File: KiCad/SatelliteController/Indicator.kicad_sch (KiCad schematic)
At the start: 22 parts

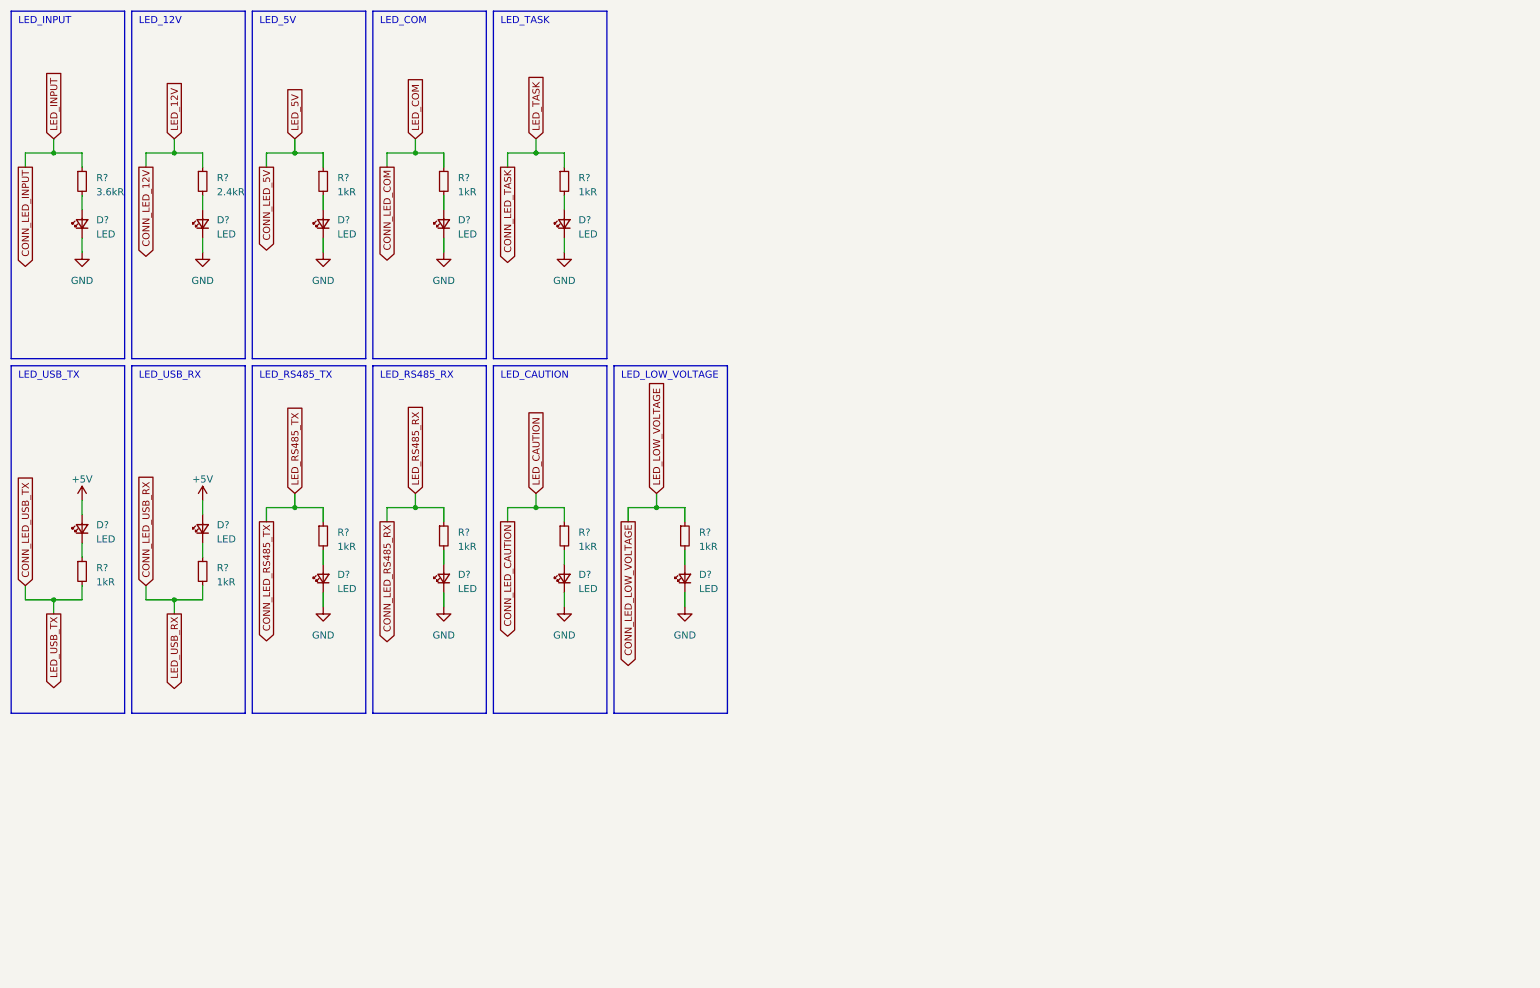
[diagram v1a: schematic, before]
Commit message: ランコンのKiCadプロジェクトをコピーしてサテコンを作成
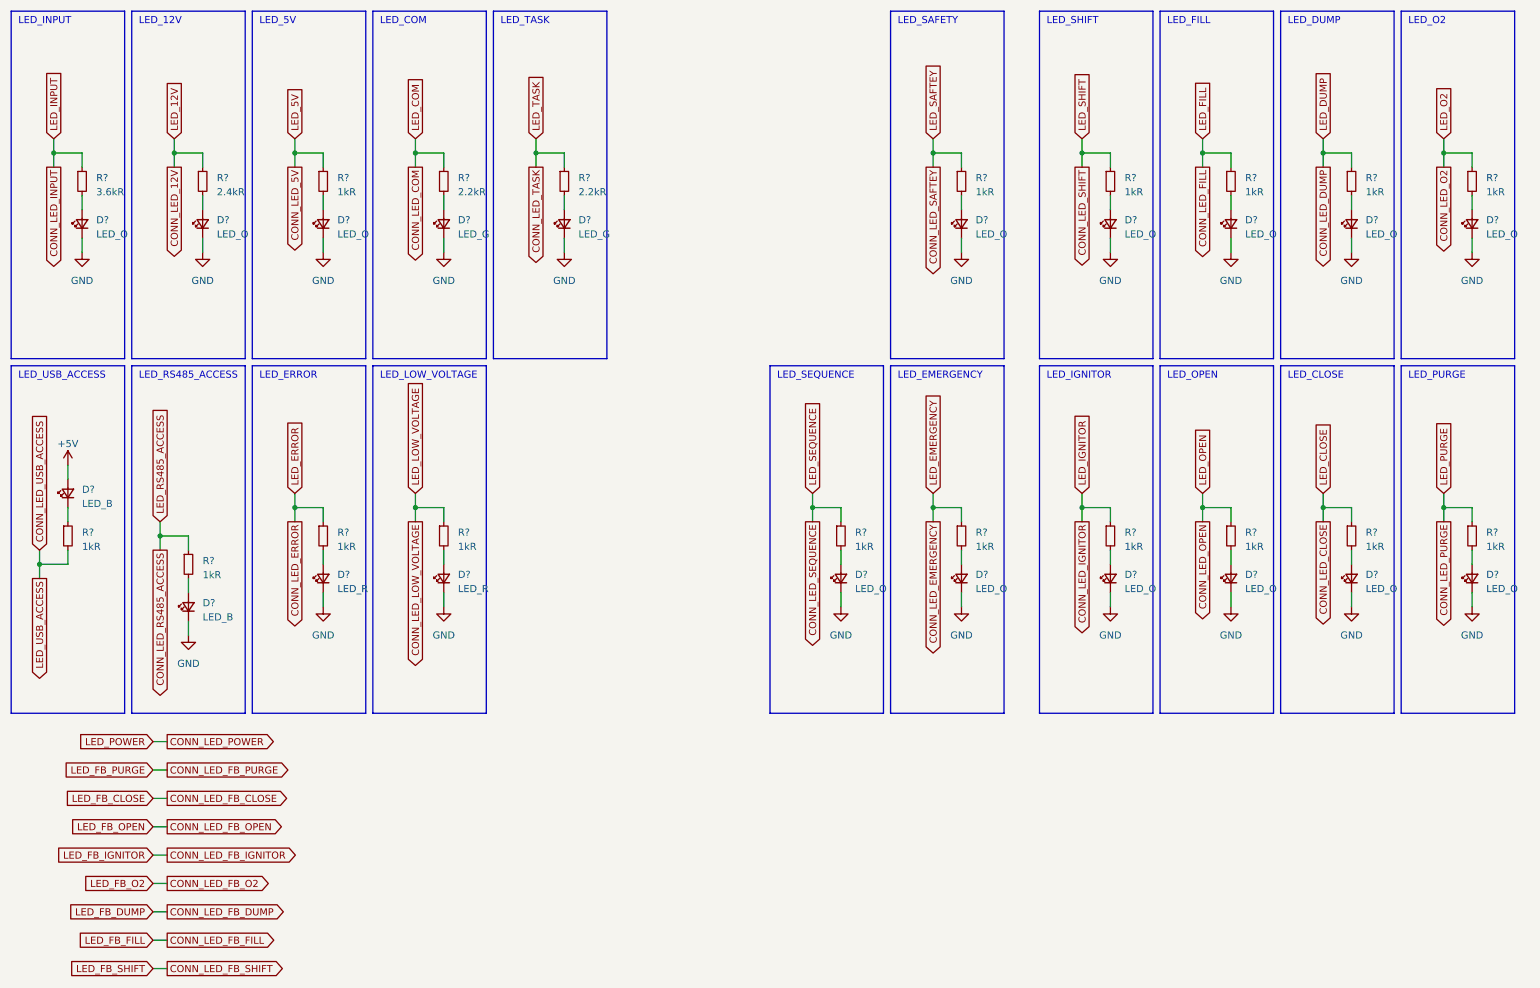
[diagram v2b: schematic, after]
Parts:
- removed D? (x2): LED, LED_SMD:LED_0603_1608Metric_Pad1.05x0.95mm_HandSolder, symbol Device:LED_Small
- removed R? (x2): 1kR, Resistor_SMD:R_0603_1608Metric_Pad0.98x0.95mm_HandSolder, symbol Device:R_Small
- added D? (x11): LED_O, LED_SMD:LED_0603_1608Metric_Pad1.05x0.95mm_HandSolder, symbol Device:LED_Small
- added R? (x11): 1kR, Resistor_SMD:R_0603_1608Metric_Pad0.98x0.95mm_HandSolder, symbol Device:R_Small
- D? (x2): value LED -> LED_R
- D? (x3): value LED -> LED_O
- D? (x2): value LED -> LED_B
- D? (x2): value LED -> LED_G
- R? (x2): value 1kR -> 2.2kR
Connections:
- net GND: now also D?.1 (K), D?.1 (K), D?.1 (K), D?.1 (K), D?.1 (K), D?.1 (K), D?.1 (K), D?.1 (K), D?.1 (K), D?.1 (K), D?.1 (K)
- net CONN_LED_CAUTION renamed CONN_LED_ERROR
- net CONN_LED_RS485_TX renamed CONN_LED_RS485_ACCESS
- net CONN_LED_USB_TX renamed CONN_LED_USB_ACCESS
- new net: D?.2 (A), R?.2 (x11)
- new net CONN_LED_CLOSE: R?.1
- new net CONN_LED_DUMP: R?.1
- new net CONN_LED_EMERGENCY: R?.1
- new net CONN_LED_FILL: R?.1
- new net CONN_LED_IGNITOR: R?.1
- new net CONN_LED_O2: R?.1
- new net CONN_LED_OPEN: R?.1
- new net CONN_LED_PURGE: R?.1
- new net CONN_LED_SAFTEY: R?.1
- new net CONN_LED_SEQUENCE: R?.1
- new net CONN_LED_SHIFT: R?.1
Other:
- note added: "LED_CLOSE"
- note added: "LED_DUMP"
- note added: "LED_EMERGENCY"
- note added: "LED_ERROR"
- note added: "LED_FILL"
- note added: "LED_IGNITOR"
- note added: "LED_O2"
- note added: "LED_OPEN"
- note added: "LED_PURGE"
- note added: "LED_RS485_ACCESS"
- note added: "LED_SAFETY"
- note added: "LED_SEQUENCE"
- note added: "LED_SHIFT"
- note added: "LED_USB_ACCESS"
- note removed: "LED_CAUTION"
- note removed: "LED_RS485_RX"
- note removed: "LED_RS485_TX"
- note removed: "LED_USB_RX"
- note removed: "LED_USB_TX"
- moved on the sheet: D?, R?

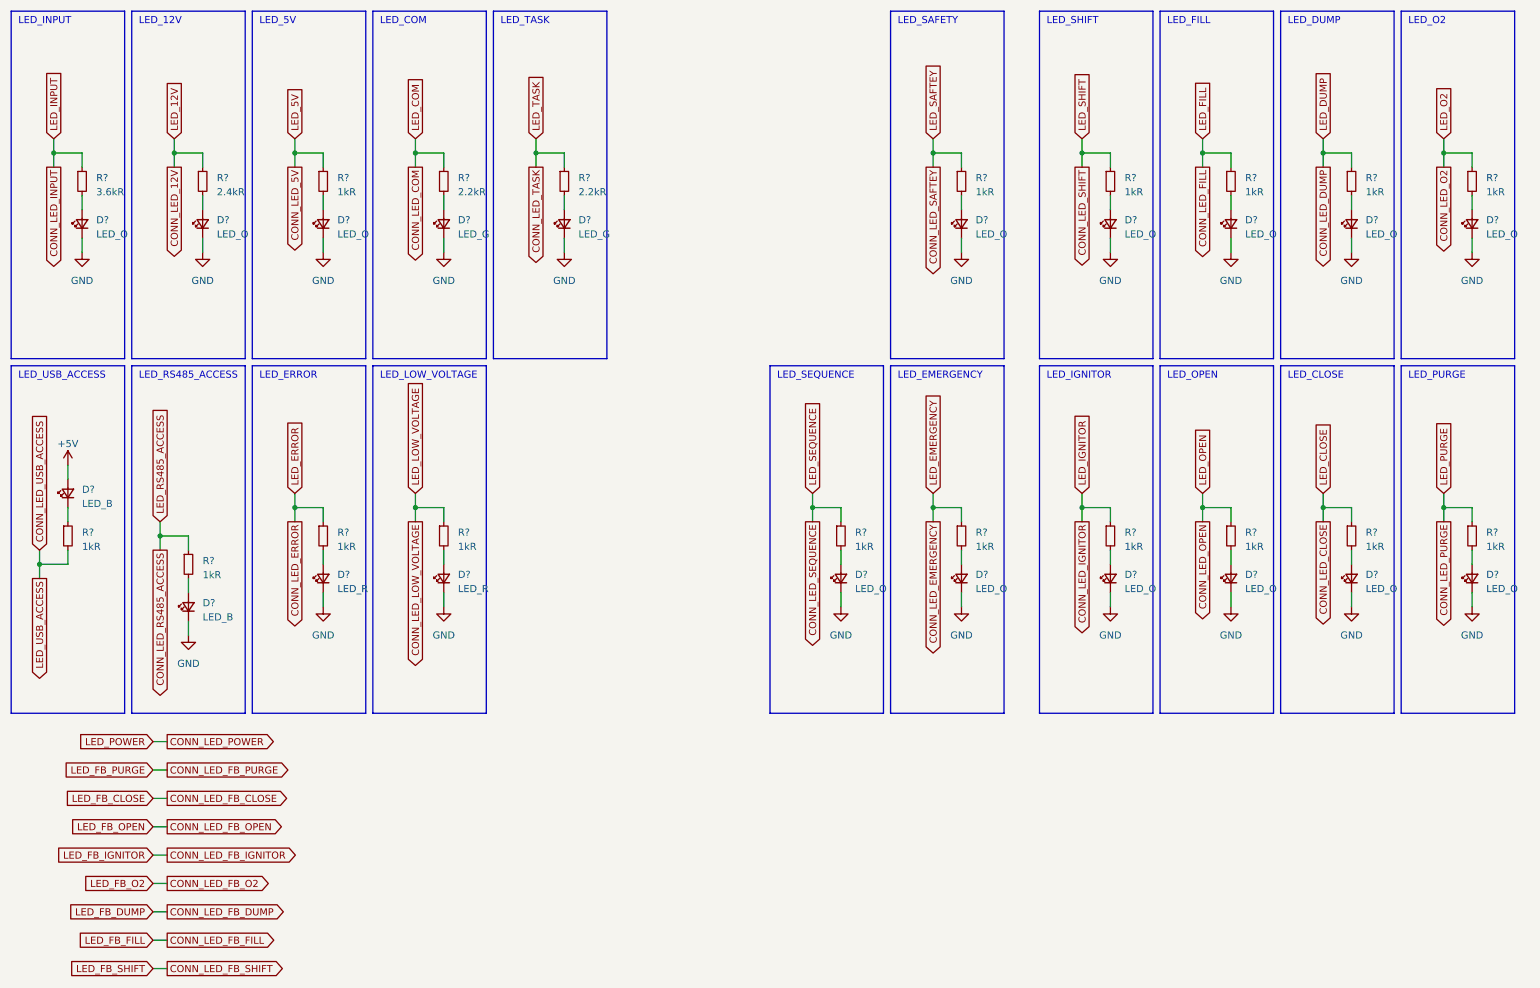
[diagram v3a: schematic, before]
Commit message: 手動操作を削除
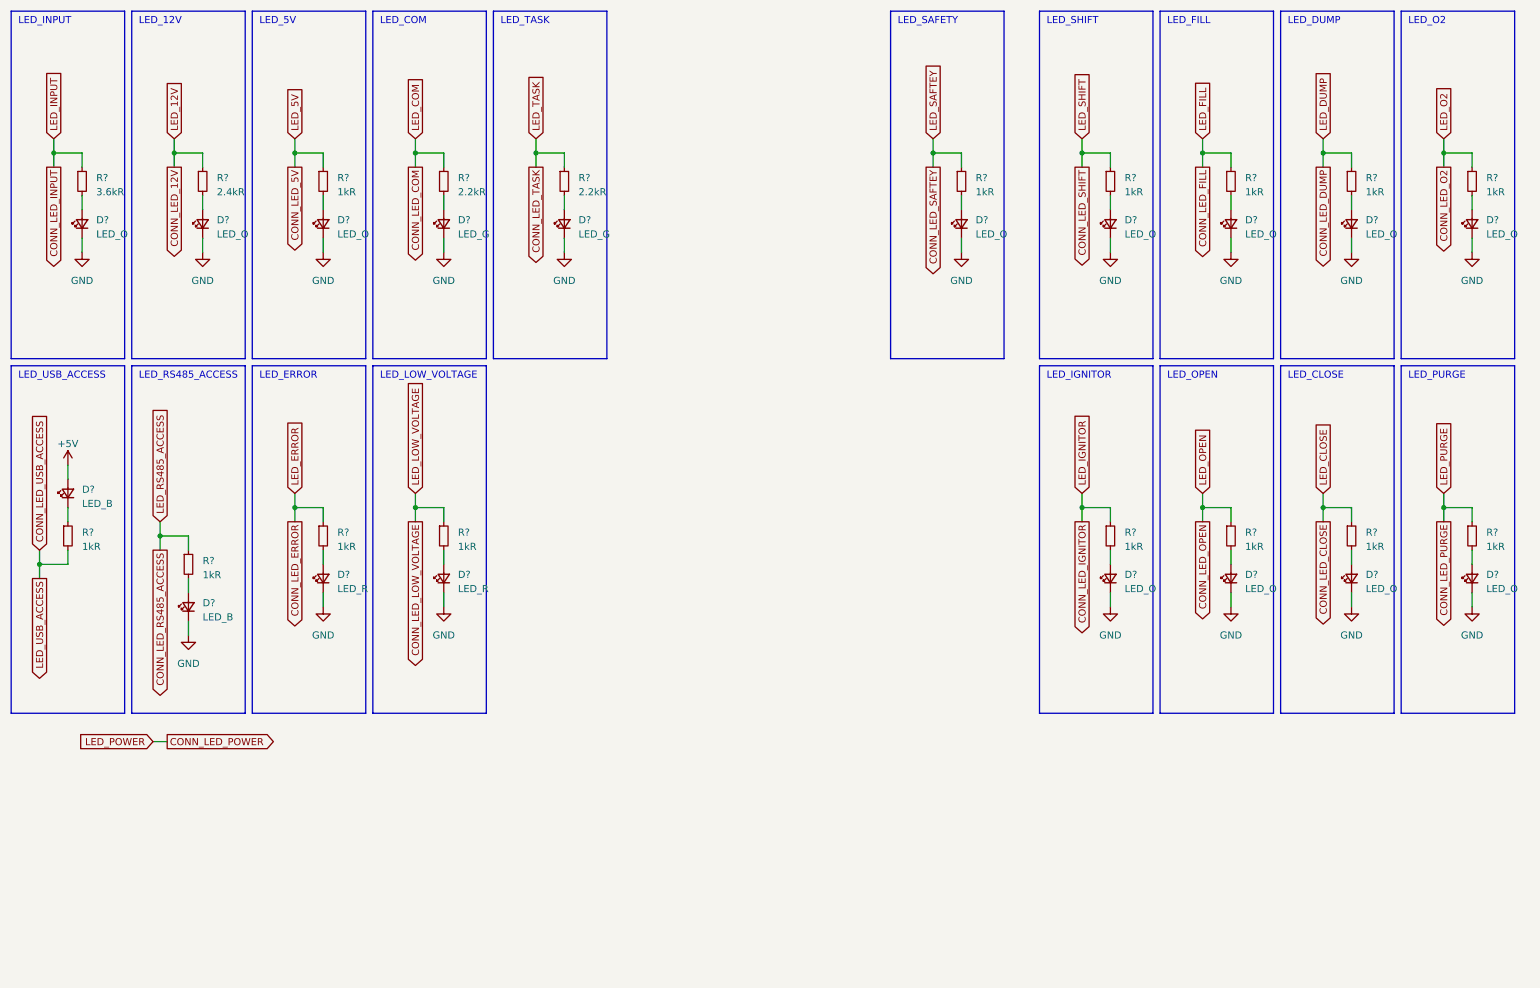
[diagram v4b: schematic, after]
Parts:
- removed D? (x2): LED_O, LED_SMD:LED_0603_1608Metric_Pad1.05x0.95mm_HandSolder, symbol Device:LED_Small
- removed R? (x2): 1kR, Resistor_SMD:R_0603_1608Metric_Pad0.98x0.95mm_HandSolder, symbol Device:R_Small
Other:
- note removed: "LED_EMERGENCY"
- note removed: "LED_SEQUENCE"

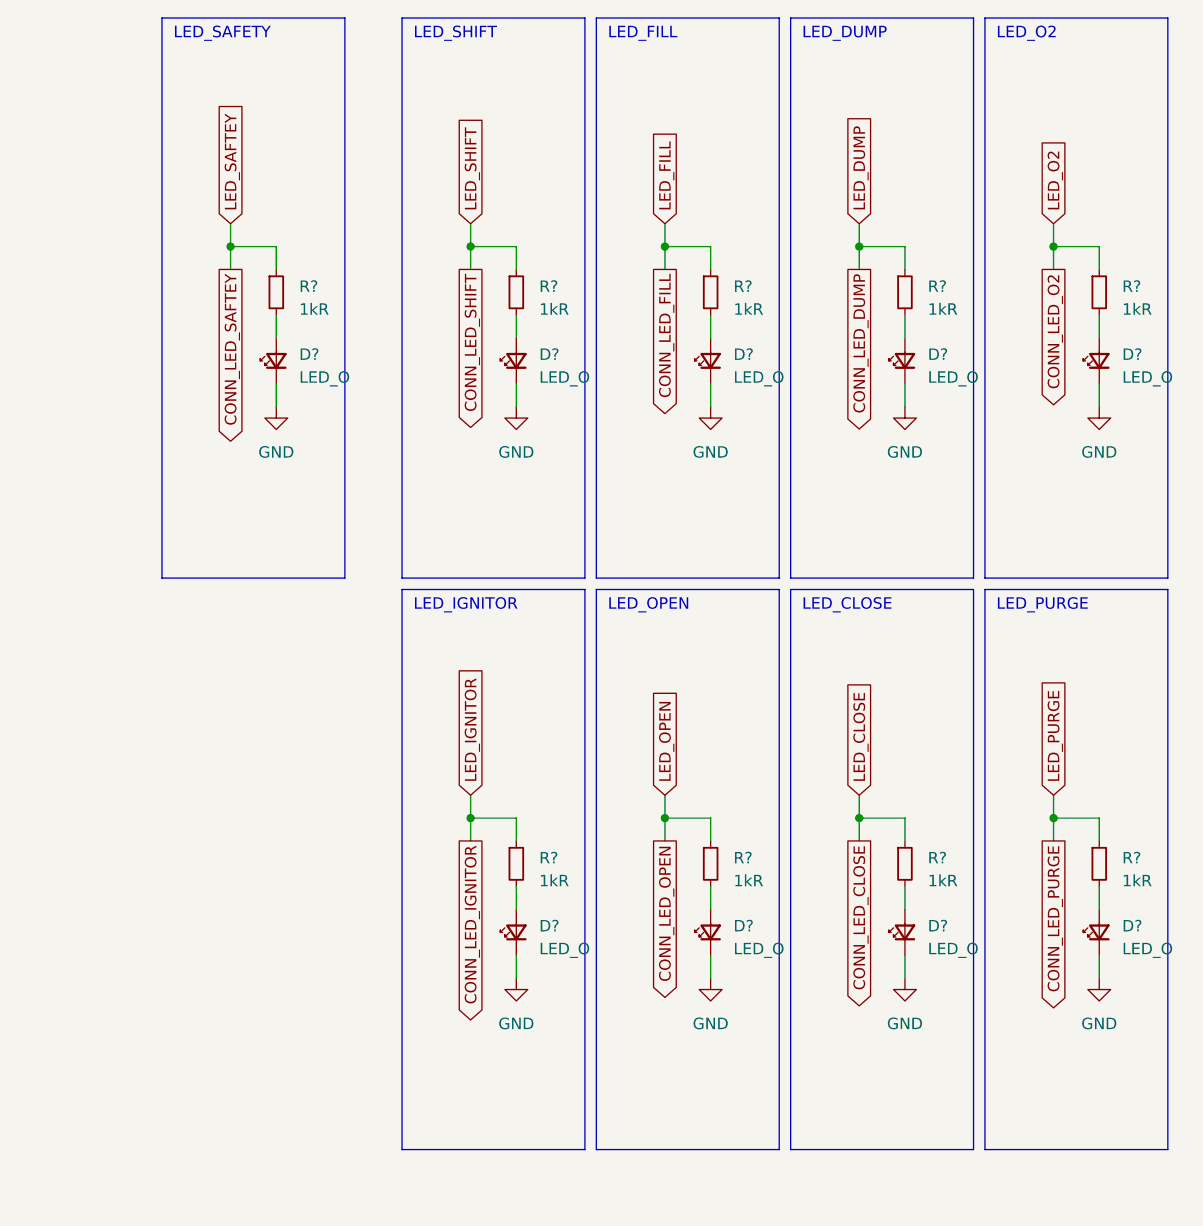
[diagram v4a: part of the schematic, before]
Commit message: サテコンの制御スイッチをプルダウンに変更
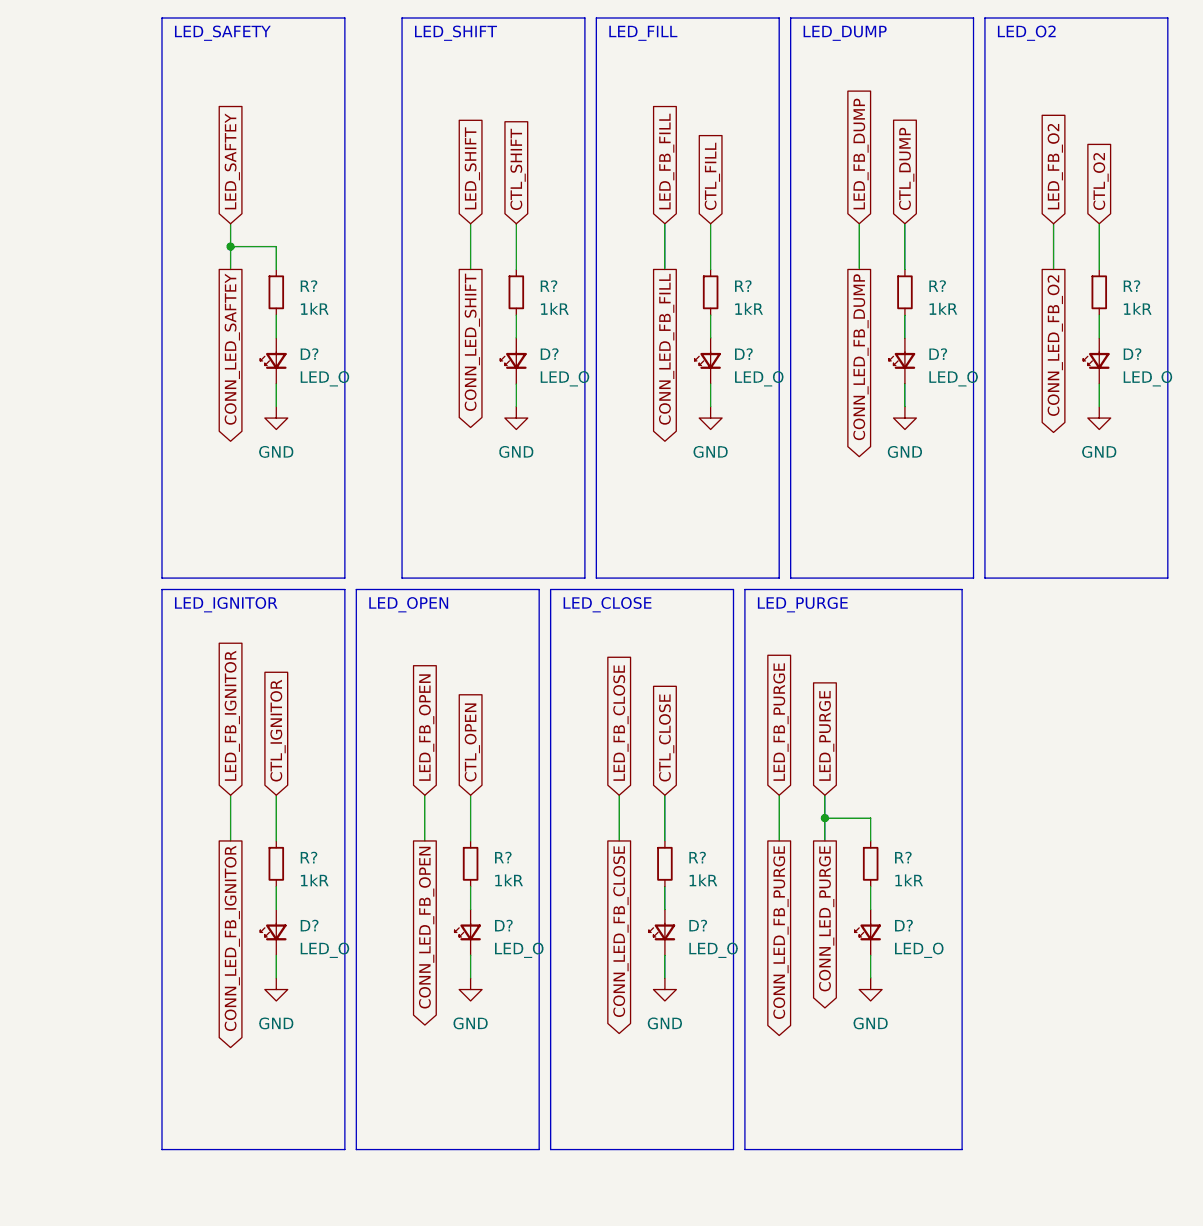
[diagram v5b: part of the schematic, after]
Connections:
- net CONN_LED_SHIFT: no longer R?.1
- net CONN_LED_CLOSE renamed CTL_CLOSE
- net CONN_LED_DUMP renamed CTL_DUMP
- net CONN_LED_FILL renamed CTL_FILL
- net CONN_LED_IGNITOR renamed CTL_IGNITOR
- net CONN_LED_O2 renamed CTL_O2
- net CONN_LED_OPEN renamed CTL_OPEN
- new net CTL_SHIFT: R?.1
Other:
- moved on the sheet: D?, R?
